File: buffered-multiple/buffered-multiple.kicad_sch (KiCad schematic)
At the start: 50 parts, among them J1 AudioJack_Switch, J10 AudioJack_Switch, J11 Conn_01x06_Pin, J12 Conn_01x06_Socket, J13 AudioJack_Switch, J14 AudioJack_Switch, J15 Conn_02x08_Odd_Even, J16 Conn_01x04_Pin, J17 Conn_01x04_Socket, J2 AudioJack_Switch, J3 AudioJack_Switch, J4 AudioJack_Switch, J5 AudioJack_Switch, J6 AudioJack_Switch, J7 Conn_01x06_Socket, J8 Conn_01x06_Pin, J9 AudioJack_Switch, U1 TL074, U2 TL072, U3 TL074

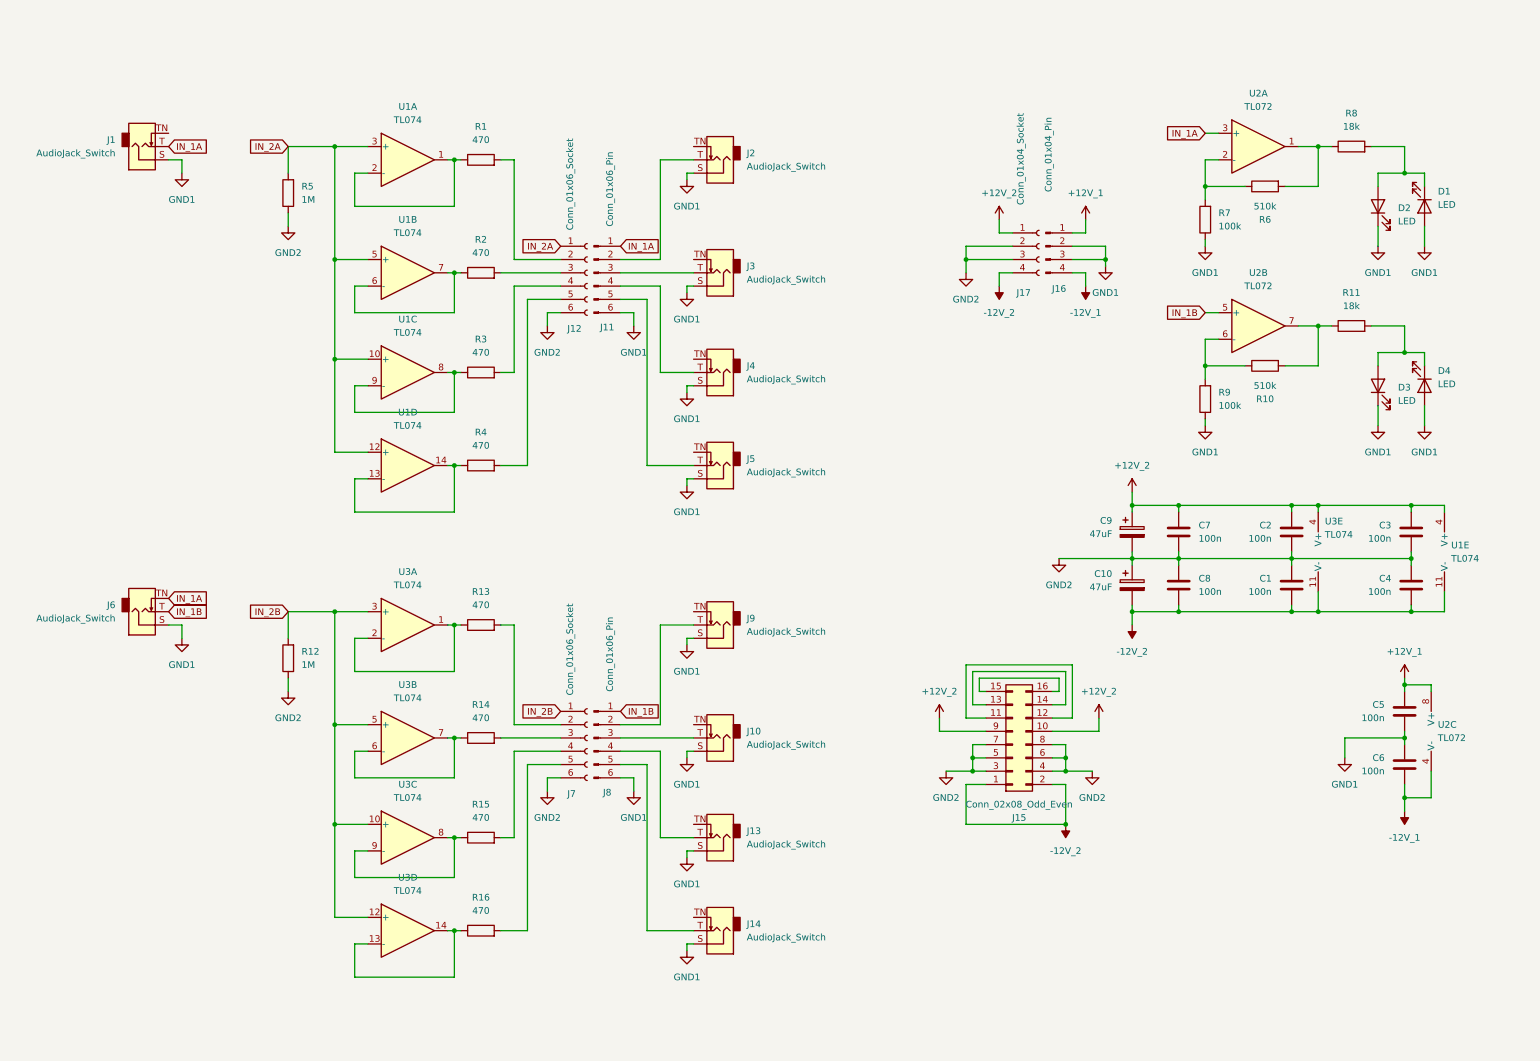
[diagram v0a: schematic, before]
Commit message: Fixed buffered multiple reversed polarity problem.
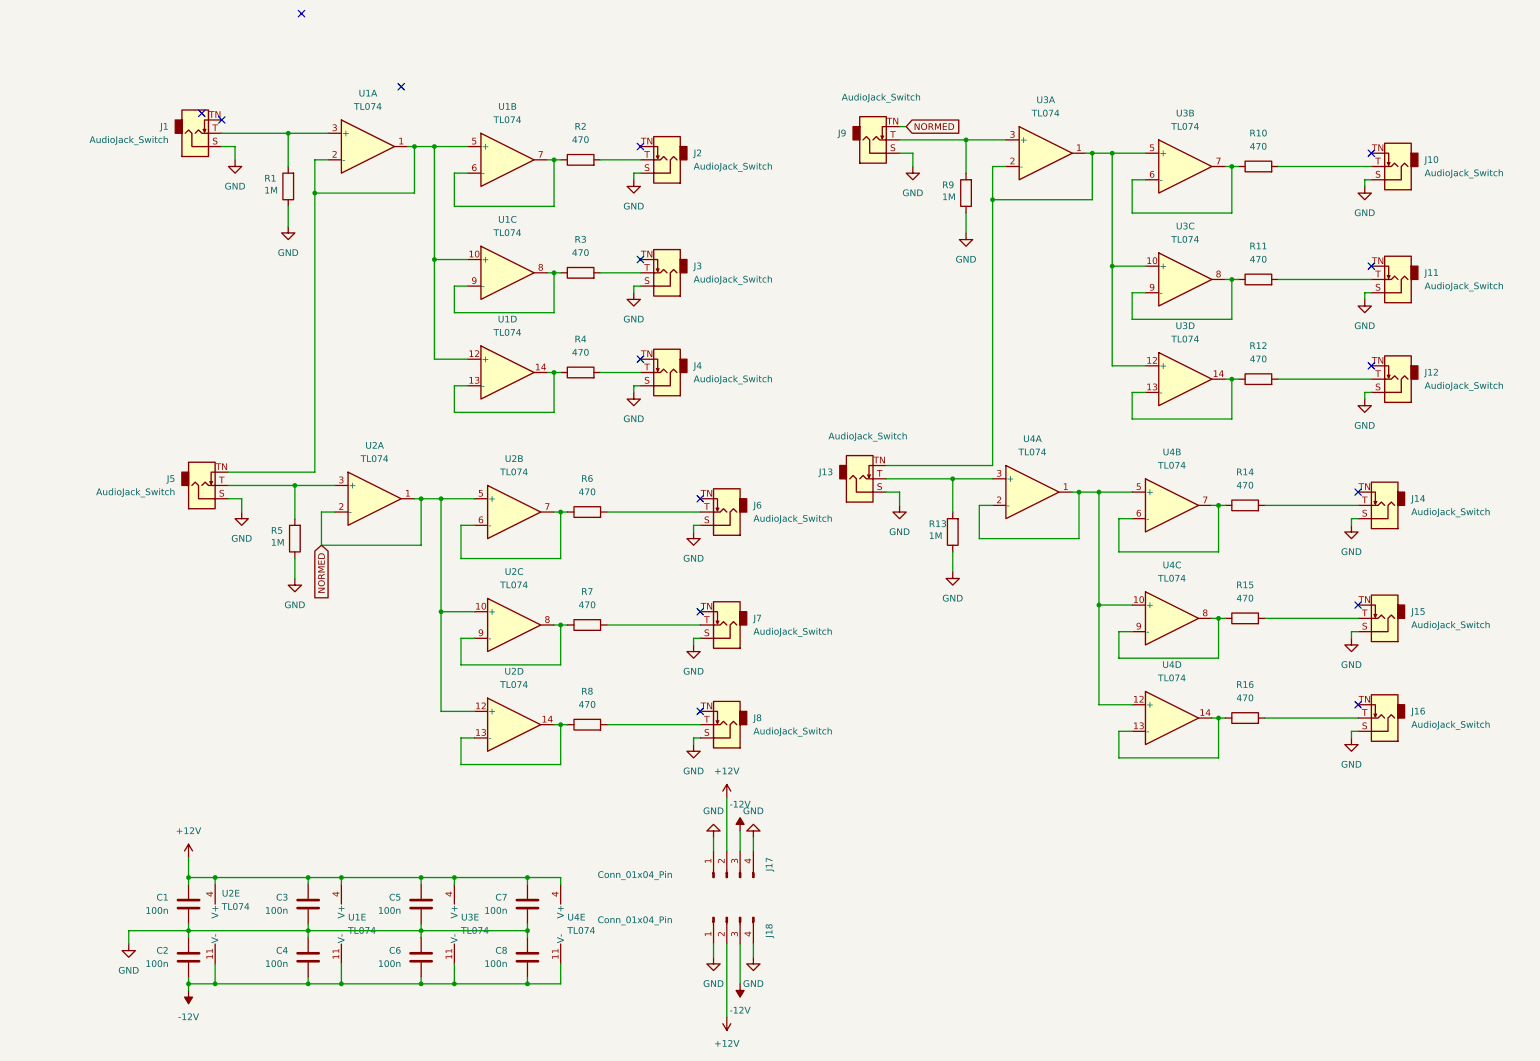
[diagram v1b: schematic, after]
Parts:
- removed C10, C9: 47uF, Capacitor_THT:CP_Radial_D10.0mm_P2.50mm_P5.00mm, symbol Device:C_Polarized
- removed D1, D2, D3, D4: LED, LED_THT:LED_D3.0mm, symbol Device:LED
- removed J11, J8: Conn_01x06_Pin, Connector_PinHeader_2.54mm:PinHeader_1x06_P2.54mm_Vertical, symbol Connector:Conn_01x06_Pin
- removed J12, J7: Conn_01x06_Socket, Connector_PinSocket_2.54mm:PinSocket_1x06_P2.54mm_Vertical, symbol Connector:Conn_01x06_Socket
- removed J15: Conn_02x08_Odd_Even, Connector_IDC:IDC-Header_2x08_P2.54mm_Vertical, symbol Connector_Generic:Conn_02x08_Odd_Even
- removed J17: Conn_01x04_Socket, Connector_PinSocket_2.54mm:PinSocket_1x04_P2.54mm_Vertical, symbol Connector:Conn_01x04_Socket
- removed R4: 470, Synth Partd:R_Axial_DIN0207_L6.3mm_D2.5mm_P7.62mm_Horizontal, symbol Device:R
- removed U2: TL072, Package_DIP:DIP-8_W7.62mm_Socket_LongPads, symbol Amplifier_Operational:TL072
- added J11, J12, J15, J16, J7, J8: AudioJack_Switch, Synth Partd:Jack_3.5mm_Switch, symbol Synth Parts:AudioJack_Switch
- added J18: Conn_01x04_Pin, Connector_PinHeader_2.54mm:PinHeader_1x04_P2.54mm_Vertical, symbol Connector:Conn_01x04_Pin
- added R5: 1M, Resistor_SMD:R_0402_1005Metric, symbol Device:R
- added unit 1 of U2
- added unit 3 of U2
- added unit 4 of U2
- added unit 2 of U2
- added unit 5 of U3
- added U4: TL074, 00_Synth Parts:SOT-23-THIN-14_2x4.2mm_P0.5mm, symbol Amplifier_Operational:TL074
- C1: renamed from C2; footprint Synth Partd:C_Rect_L7.0mm_W2.0mm_P5.00mm -> Capacitor_SMD:C_0402_1005Metric
- C2: renamed from C1; footprint Synth Partd:C_Rect_L7.0mm_W2.0mm_P5.00mm -> Capacitor_SMD:C_0402_1005Metric
- C3, C4, C5, C6, C7, C8: footprint Synth Partd:C_Rect_L7.0mm_W2.0mm_P5.00mm -> Capacitor_SMD:C_0402_1005Metric
- R1: renamed from R5; footprint Synth Partd:R_Axial_DIN0207_L6.3mm_D2.5mm_P7.62mm_Horizontal -> Resistor_SMD:R_0402_1005Metric
- R10, R6: value 510k -> 470; footprint Synth Partd:R_Axial_DIN0207_L6.3mm_D2.5mm_P7.62mm_Horizontal -> Resistor_SMD:R_0402_1005Metric
- R11, R8: value 18k -> 470; footprint Synth Partd:R_Axial_DIN0207_L6.3mm_D2.5mm_P7.62mm_Horizontal -> Resistor_SMD:R_0402_1005Metric
- R12: value 1M -> 470; footprint Synth Partd:R_Axial_DIN0207_L6.3mm_D2.5mm_P7.62mm_Horizontal -> Resistor_SMD:R_0402_1005Metric
- R13: value 470 -> 1M; footprint Synth Partd:R_Axial_DIN0207_L6.3mm_D2.5mm_P7.62mm_Horizontal -> Resistor_SMD:R_0402_1005Metric
- R14, R15, R16: footprint Synth Partd:R_Axial_DIN0207_L6.3mm_D2.5mm_P7.62mm_Horizontal -> Resistor_SMD:R_0402_1005Metric
- R2: renamed from R1; footprint Synth Partd:R_Axial_DIN0207_L6.3mm_D2.5mm_P7.62mm_Horizontal -> Resistor_SMD:R_0402_1005Metric
- R3: renamed from R2; footprint Synth Partd:R_Axial_DIN0207_L6.3mm_D2.5mm_P7.62mm_Horizontal -> Resistor_SMD:R_0402_1005Metric
- R4: renamed from R3; footprint Synth Partd:R_Axial_DIN0207_L6.3mm_D2.5mm_P7.62mm_Horizontal -> Resistor_SMD:R_0402_1005Metric
- R7: value 100k -> 470; footprint Synth Partd:R_Axial_DIN0207_L6.3mm_D2.5mm_P7.62mm_Horizontal -> Resistor_SMD:R_0402_1005Metric
- R9: value 100k -> 1M; footprint Synth Partd:R_Axial_DIN0207_L6.3mm_D2.5mm_P7.62mm_Horizontal -> Resistor_SMD:R_0402_1005Metric
- U1, U3: footprint Package_DIP:DIP-14_W7.62mm_Socket_LongPads -> 00_Synth Parts:SOT-23-THIN-14_2x4.2mm_P0.5mm
- U2: renamed from U3; footprint Package_DIP:DIP-14_W7.62mm_Socket_LongPads -> 00_Synth Parts:SOT-23-THIN-14_2x4.2mm_P0.5mm
- renumbered J16 to J17
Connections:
- net +12V_2 is gone; now on net +12V: C1.1, C3.1, C7.1, U1.4 (V+), U2.4 (V+)
- net -12V_2 is gone; now on net -12V: C2.2, C4.2, C8.2, U1.11 (V-), U2.11 (V-)
- net IN_1B is gone; now on an unnamed net: J6.T
- net at U1.1, U1.2 (-): now also J5.TN, U1.10 (+), U1.12 (+), U1.5 (+); no longer R2.1
- net at U3.1, U3.2 (-): now also J13.TN, U3.10 (+), U3.12 (+), U3.5 (+); no longer R13.1
- net at R13.2: now also J13.T, U4.3 (+)
- net at U1.6 (-), U1.7: now also R2.1; no longer R3.1
- net at R3.2: now also J3.T
- net at R2.2: now also J2.T
- net at J4.T: now also R4.2
- net at U3.6 (-), U3.7: now also R10.1; no longer R14.1
- net at J10.T: now also R10.2
- net at U1.8, U1.9 (-): now also R3.1; no longer R4.1
- net at R11.2: now also J11.T
- net at R6.2: no longer R8.1
- net at R6.1: now also U2.6 (-), U2.7; no longer R7.2
- net at R14.2: now also J14.T
- net at R9.2: now also J9.T, U3.3 (+); no longer R10.1
- net at U3.8, U3.9 (-): now also R11.1; no longer R15.1
- net at J5.T: now also R5.2, U2.3 (+)
- net at R8.2: now also J8.T
- net at U3.13 (-), U3.14: now also R12.1; no longer R16.1
- net NORMED: now reaches J9.TN
- net NORMED: now also U2.1, U2.10 (+), U2.12 (+), U2.2 (-), U2.5 (+)
- net at R15.2: now also J15.T
- net at U1.13 (-), U1.14: now also R4.1
- net at R16.2: now also J16.T
- net +12V_1 renamed +12V
- net +12V: now also J17.2 (Pin_2), J18.2 (Pin_2), U3.4 (V+), U4.4 (V+); no longer J17.1 (Pin_1)
- net -12V_1 renamed -12V
- net -12V: now also J17.3 (Pin_3), J18.3 (Pin_3), U3.11 (V-), U4.11 (V-); no longer J17.4 (Pin_4)
- net GND1 renamed GND
- net GND: now also C1.2, C2.1, C3.2, C4.1, C7.2, C8.1, J17.1 (Pin_1), J17.4 (Pin_4), R1.1, R13.1, J11.S, J12.S, J15.S, J16.S, J18.1 (Pin_1), J18.4 (Pin_4), J7.S, J8.S, R5.1; no longer J17.2 (Pin_2), J17.3 (Pin_3), R7.1
- removed net GND2: C1.2, C2.1, C3.2, C4.1, C7.2, C8.1, R1.1, R12.1
- net IN_1A: no longer names the net of J6.TN
- net IN_1A: no longer J1.T
- removed net IN_2A: R1.2, U1.10 (+), U1.12 (+), U1.3 (+), U1.5 (+)
- removed net IN_2B: R12.2, U3.10 (+), U3.12 (+), U3.3 (+), U3.5 (+)
- new net: J1.T, R1.2, U1.3 (+)
- new net: U4.1, U4.10 (+), U4.12 (+), U4.2 (-), U4.5 (+)
- new net: R15.1, U4.8, U4.9 (-)
- new net: R8.1, U2.13 (-), U2.14
- new net: R7.1, U2.8, U2.9 (-)
- new net: J7.T, R7.2
- new net: J12.T, R12.2
- new net: R16.1, U4.13 (-), U4.14
- new net: R14.1, U4.6 (-), U4.7
- no-connect marks 0 -> 16
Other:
- moved on the sheet: C1, C2, C3, C4, J1, J17, J2, J3, J4, R1, R2, R3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
